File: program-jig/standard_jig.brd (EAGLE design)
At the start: 19.8 x 65.1 mm, 12 parts, among them J4 455-1750-1-ND, J5 6_PIN_SERIAL_CABLEPTH, U1 3.3V/150mA

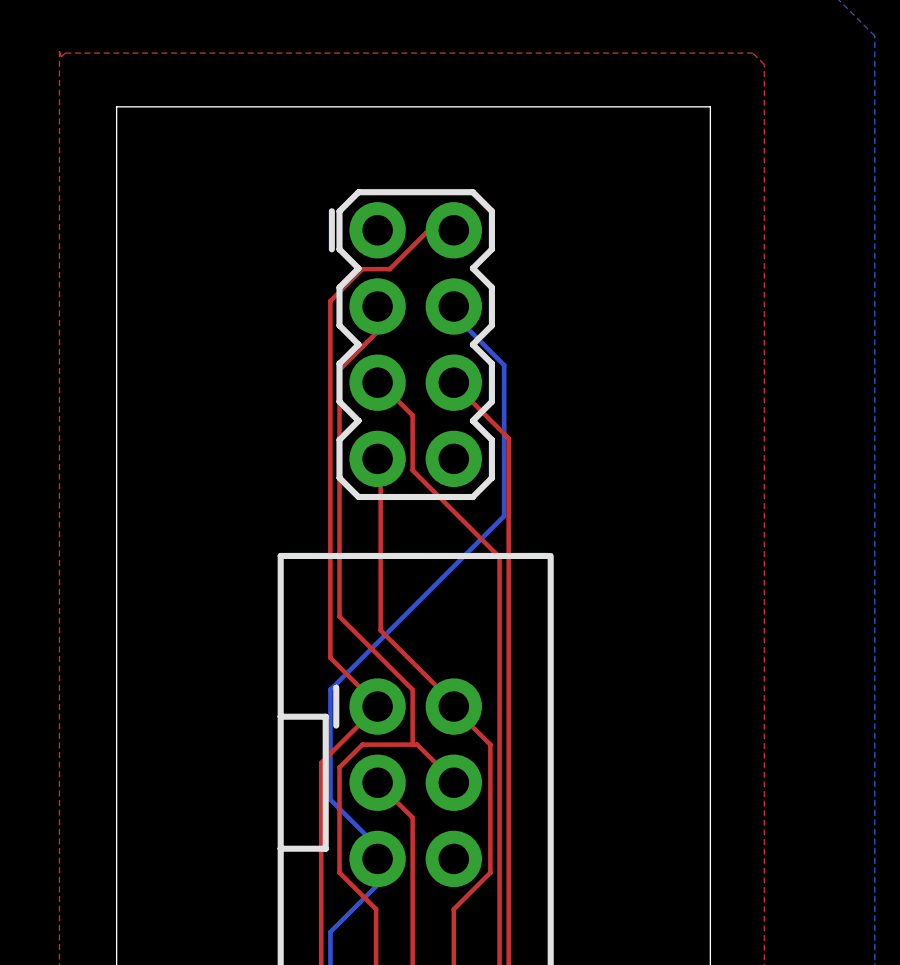
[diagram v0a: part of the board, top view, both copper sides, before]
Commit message: Optional pullup on I2C + Default I2C0
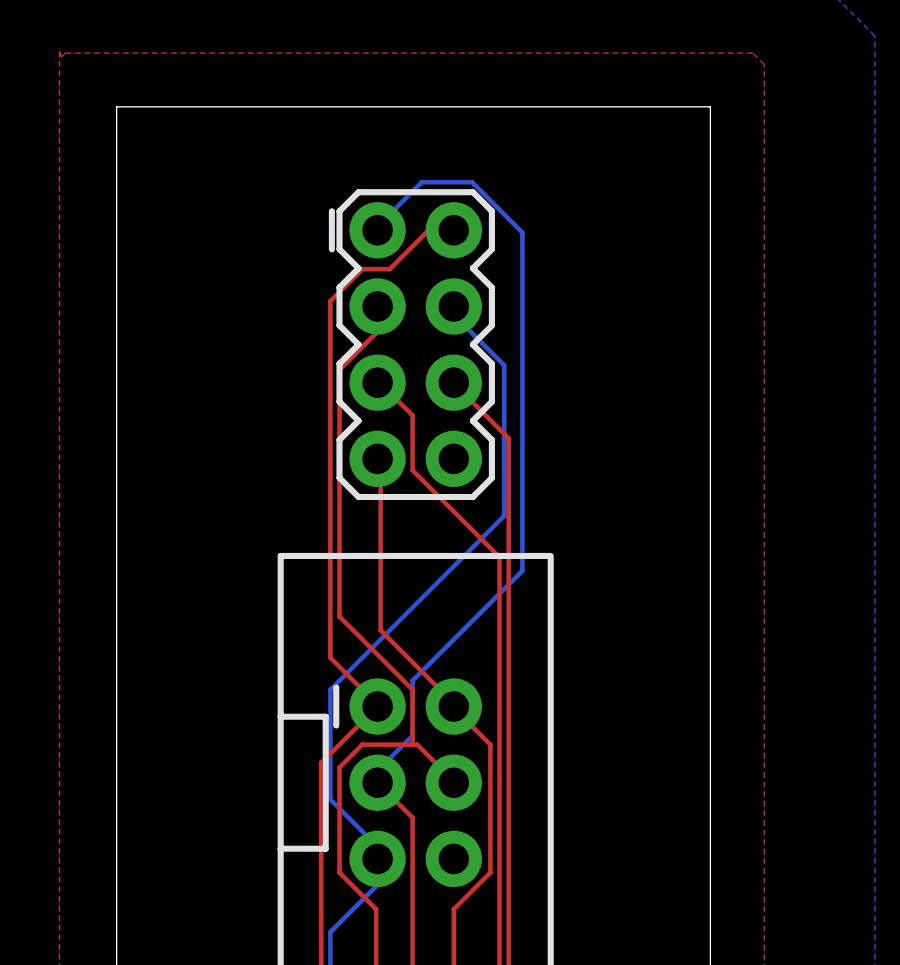
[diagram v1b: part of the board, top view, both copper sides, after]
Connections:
- removed net CSK: J3.1
- net SCK: now also J3.1
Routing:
- net SCK: track 20.0 -> 46.7 mm
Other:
- board text added: "Version 1.0"
- board text removed: "Version 0.5"
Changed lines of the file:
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@@
 <?xml version="1.0" encoding="utf-8"?>
 <!DOCTYPE eagle SYSTEM "eagle.dtd">
-<eagle version="9.0.0">
+<eagle version="9.1.1">
 <drawing>
 <settings>
@@
 <dimension x1="19.9825" y1="82.22" x2="0.1905" y2="82.22" x3="10.0865" y3="86.0425" textsize="0.9144" textratio="5" layer="51"/>
 <text x="18.415" y="50.165" size="1.1176" layer="28" font="vector" ratio="5" rot="MR270">WaggleNet Pogo Jig</text>
-<text x="16.51" y="41.91" size="0.8128" layer="28" font="vector" ratio="5" rot="MR270">Version 0.5</text>
+<text x="16.51" y="41.91" size="0.8128" layer="28" font="vector" ratio="5" rot="MR270">Version 1.0</text>
 <text x="18.415" y="80.01" size="0.9144" layer="28" font="vector" ratio="5" rot="MR270">(c) Jimmy He, Sunmola Orealuwa
 University of Illinois at Urbana-Champaign</text>
@@
 <param name="checkStop" value="0"/>
 <param name="checkValues" value="0"/>
+<param name="checkNames" value="1"/>
+<param name="checkWireStubs" value="1"/>
+<param name="checkPolygonWidth" value="0"/>
 <param name="useDiameter" value="13"/>
 <param name="maxErrors" value="50"/>
@@
 <wire x1="8.89" y1="59.69" x2="10.0584" y2="58.5216" width="0.1524" layer="1"/>
 <wire x1="8.9916" y1="40.6908" x2="8.89" y2="40.64" width="0.1524" layer="1"/>
+<contactref element="J3" pad="1"/>
+<wire x1="9.4488" y1="78.6384" x2="8.9916" y2="78.1812" width="0.1524" layer="16"/>
+<wire x1="9.4488" y1="78.7908" x2="9.4488" y2="78.6384" width="0.1524" layer="16"/>
+<wire x1="10.3632" y1="79.7052" x2="9.4488" y2="78.7908" width="0.1524" layer="16"/>
+<wire x1="12.0396" y1="79.7052" x2="10.3632" y2="79.7052" width="0.1524" layer="16"/>
+<wire x1="13.716" y1="78.0288" x2="12.0396" y2="79.7052" width="0.1524" layer="16"/>
+<wire x1="13.716" y1="66.7512" x2="13.716" y2="78.0288" width="0.1524" layer="16"/>
+<wire x1="10.0584" y1="63.0936" x2="13.716" y2="66.7512" width="0.1524" layer="16"/>
+<wire x1="10.0584" y1="61.2648" x2="10.0584" y2="63.0936" width="0.1524" layer="16"/>
+<wire x1="8.9916" y1="60.198" x2="10.0584" y2="61.2648" width="0.1524" layer="16"/>
+<wire x1="8.9916" y1="59.7408" x2="8.9916" y2="60.198" width="0.1524" layer="16"/>
+<wire x1="8.9916" y1="78.1812" x2="8.89" y2="78.105" width="0.1524" layer="16"/>
+<wire x1="8.9916" y1="59.7408" x2="8.89" y2="59.69" width="0.1524" layer="16"/>
 </signal>
 <signal name="RST">
@@
 <wire x1="8.9916" y1="72.9996" x2="8.89" y2="73.025" width="0.1524" layer="1"/>
 </signal>
-<signal name="CSK">
-<contactref element="J3" pad="1"/>
-</signal>
 <signal name="N$1">
 <contactref element="D1" pad="C"/>
@@
 </signal>
 </signals>
+<mfgpreviewcolors>
+<mfgpreviewcolor name="soldermaskcolor" color="0xC8008000"/>
+<mfgpreviewcolor name="silkscreencolor" color="0xFFFEFEFE"/>
+<mfgpreviewcolor name="backgroundcolor" color="0xFF282828"/>
+<mfgpreviewcolor name="coppercolor" color="0xFFFFBF00"/>
+<mfgpreviewcolor name="substratecolor" color="0xFF786E46"/>
+</mfgpreviewcolors>
 </board>
 </drawing>
